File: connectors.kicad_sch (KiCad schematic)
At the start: 1 part, among them J4 UJ20-C-V-SMT-TR-68

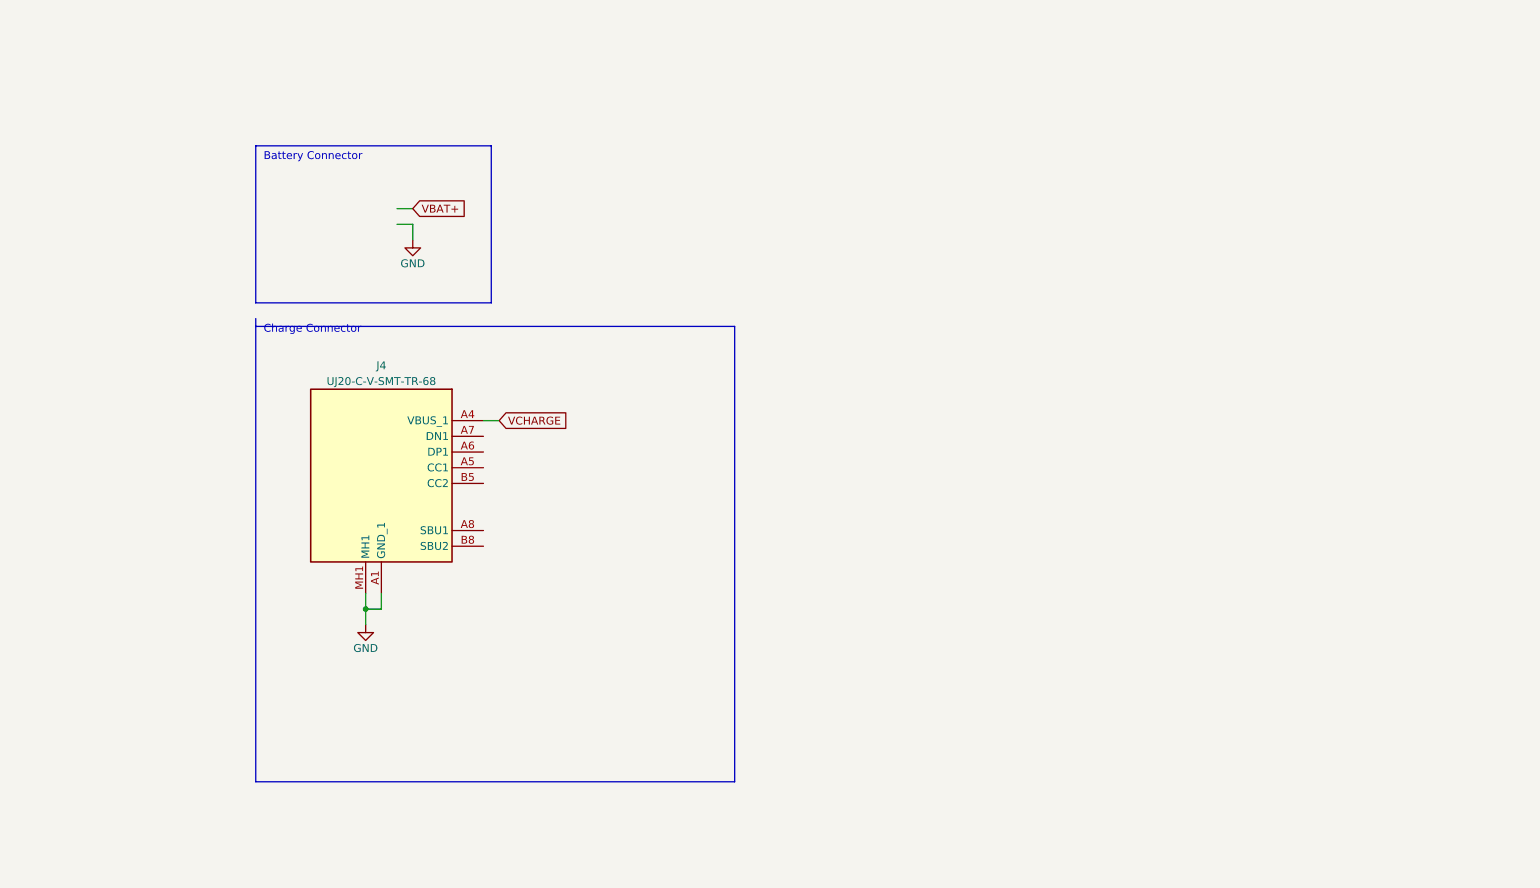
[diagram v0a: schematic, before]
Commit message: added usb protection
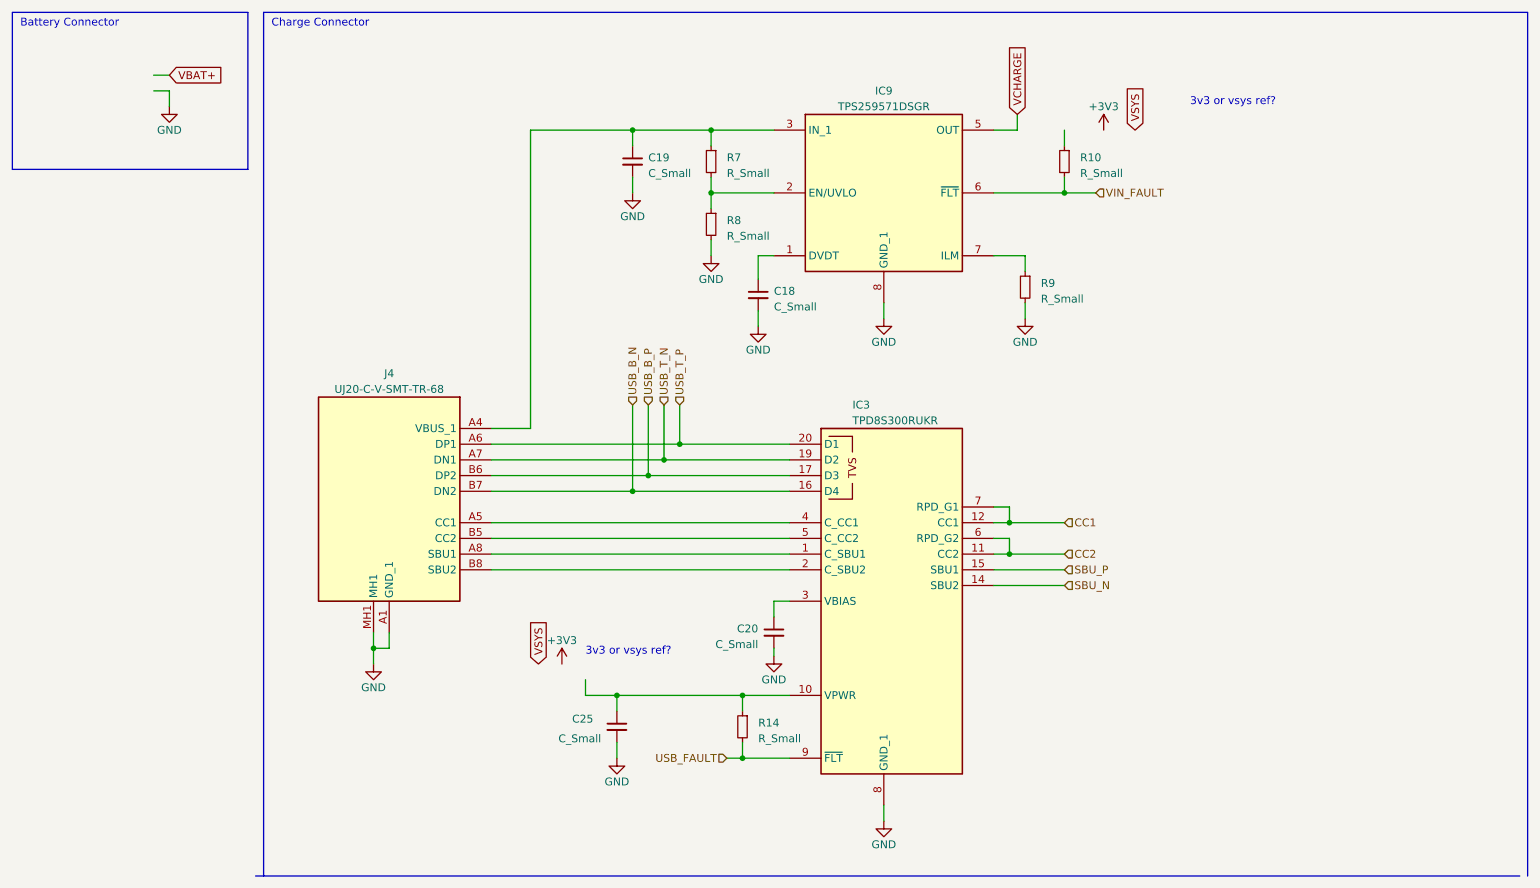
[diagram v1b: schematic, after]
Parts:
- added C18, C19, C20, C25: C_Small, symbol Device:C_Small
- added IC3: TPD8S300RUKR, ARMband:QFN40P300X300X80-21N-D, symbol ARMband:TPD8S300RUKR
- added IC9: TPS259571DSGR, SON50P200X200X80-9N, symbol LibraryLoader:TPS259571DSGR
- added R10, R14, R7, R8, R9: R_Small, symbol Device:R_Small
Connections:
- net GND: now also C18.2, C19.2, C20.2, C25.2, IC3.13 (GND_2), IC3.18 (GND_3), IC3.21 (GND_4), IC3.8 (GND_1), IC9.8 (GND_1), IC9.9 (GND_2), R8.2, R9.2
- net VCHARGE: now also IC9.5 (OUT); no longer J4.A4 (VBUS_1), J4.A9 (VBUS_2), J4.B4 (VBUS_3), J4.B9 (VBUS_4)
- net at J4.A5 (CC1): now also IC3.4 (C_CC1)
- net USB_B_P: now reaches J4.B6 (DP2)
- net USB_B_P: now also IC3.17 (D3); no longer J4.A6 (DP1)
- net USB_B_N: now reaches J4.B7 (DN2)
- net USB_B_N: now also IC3.16 (D4); no longer J4.A7 (DN1)
- net at J4.A8 (SBU1): now also IC3.1 (C_SBU1)
- net at J4.B5 (CC2): now also IC3.5 (C_CC2)
- net at J4.B8 (SBU2): now also IC3.2 (C_SBU2)
- new net: C25.1, IC3.10 (VPWR), R14.1
- new net: IC9.2 (EN/UVLO), R7.2, R8.1
- new net: C19.1, IC9.3 (IN_1), IC9.4 (IN_2), J4.A4 (VBUS_1), J4.A9 (VBUS_2), J4.B4 (VBUS_3), J4.B9 (VBUS_4), R7.1
- new net: C18.1, IC9.1 (DVDT)
- new net: IC9.7 (ILM), R9.1
- new net: C20.1, IC3.3 (VBIAS)
- new net CC1: IC3.12 (CC1), IC3.7 (RPD_G1)
- new net CC2: IC3.11 (CC2), IC3.6 (RPD_G2)
- new net SBU_N: IC3.14 (SBU2)
- new net SBU_P: IC3.15 (SBU1)
- new net USB_FAULT: IC3.9 (~{FLT}), R14.2
- new net USB_T_N: IC3.19 (D2), J4.A7 (DN1)
- new net USB_T_P: IC3.20 (D1), J4.A6 (DP1)
- new net VIN_FAULT: IC9.6 (~{FLT}), R10.2
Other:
- note added: "3v3 or vsys ref?"

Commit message: Update capacitor values
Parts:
- C18: value C_Small -> 3.3nF
- C19: value C_Small -> 0.1uF
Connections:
- net +3V3: now also R10.1
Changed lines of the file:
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@@
       (effects (font (size 1.27 1.27)) (justify right))
     )
-    (property "Value" "C_Small" (at 125.73 51.4413 0)
+    (property "Value" "0.1uF" (at 125.73 51.4413 0)
       (effects (font (size 1.27 1.27)) (justify right))
     )
@@
     )
   )
-  (symbol (lib_id "power:+3V3") (at 199.39 44.45 0) (unit 1)
+  (symbol (lib_id "power:+3V3") (at 193.04 44.45 0) (unit 1)
     (in_bom yes) (on_board yes) (dnp no) (fields_autoplaced)
-    (property "Reference" "#PWR062" (at 199.39 48.26 0)
-      (effects (font (size 1.27 1.27)) hide)
-    )
-    (property "Value" "+3V3" (at 199.39 40.64 0)
-      (effects (font (size 1.27 1.27)))
-    )
-    (property "Footprint" "" (at 199.39 44.45 0)
-      (effects (font (size 1.27 1.27)) hide)
-    )
-    (property "Datasheet" "" (at 199.39 44.45 0)
+    (property "Reference" "#PWR062" (at 193.04 48.26 0)
+      (effects (font (size 1.27 1.27)) hide)
+    )
+    (property "Value" "+3V3" (at 193.04 40.64 0)
+      (effects (font (size 1.27 1.27)))
+    )
+    (property "Footprint" "" (at 193.04 44.45 0)
+      (effects (font (size 1.27 1.27)) hide)
+    )
+    (property "Datasheet" "" (at 193.04 44.45 0)
       (effects (font (size 1.27 1.27)) hide)
     )
@@
       (effects (font (size 1.27 1.27)) (justify right))
     )
-    (property "Value" "C_Small" (at 146.05 73.0313 0)
-      (effects (font (size 1.27 1.27)) (justify right))
-    )
+    (property "Value" "3.3nF" (at 146.05 73.0313 0)
+      (effects (font (size 1.27 1.27)) (justify right))
+    )
